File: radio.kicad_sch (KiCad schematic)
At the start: 34 parts

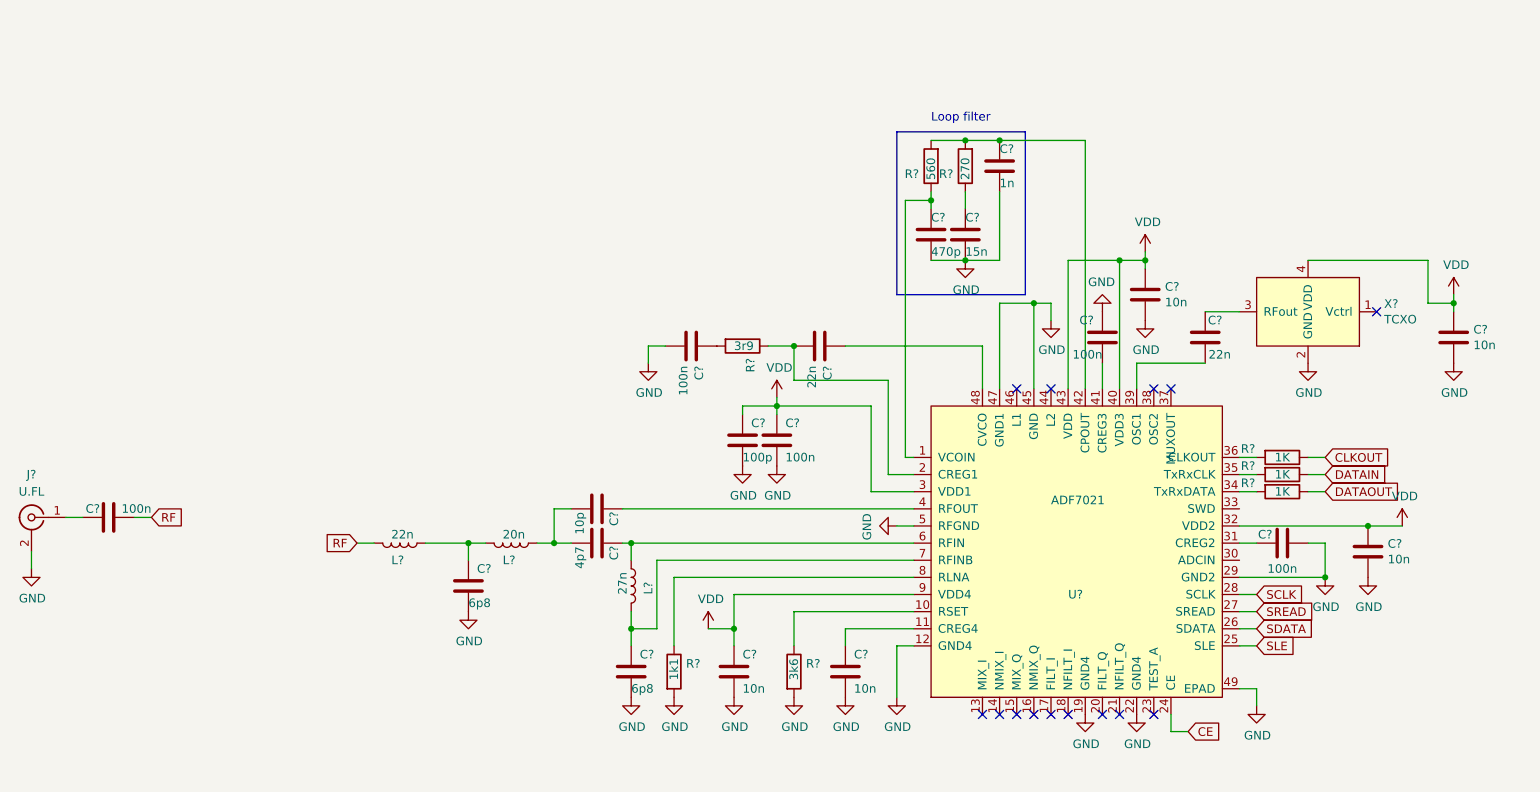
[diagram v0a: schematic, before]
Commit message: Changed MCU and M.2 pin assignment
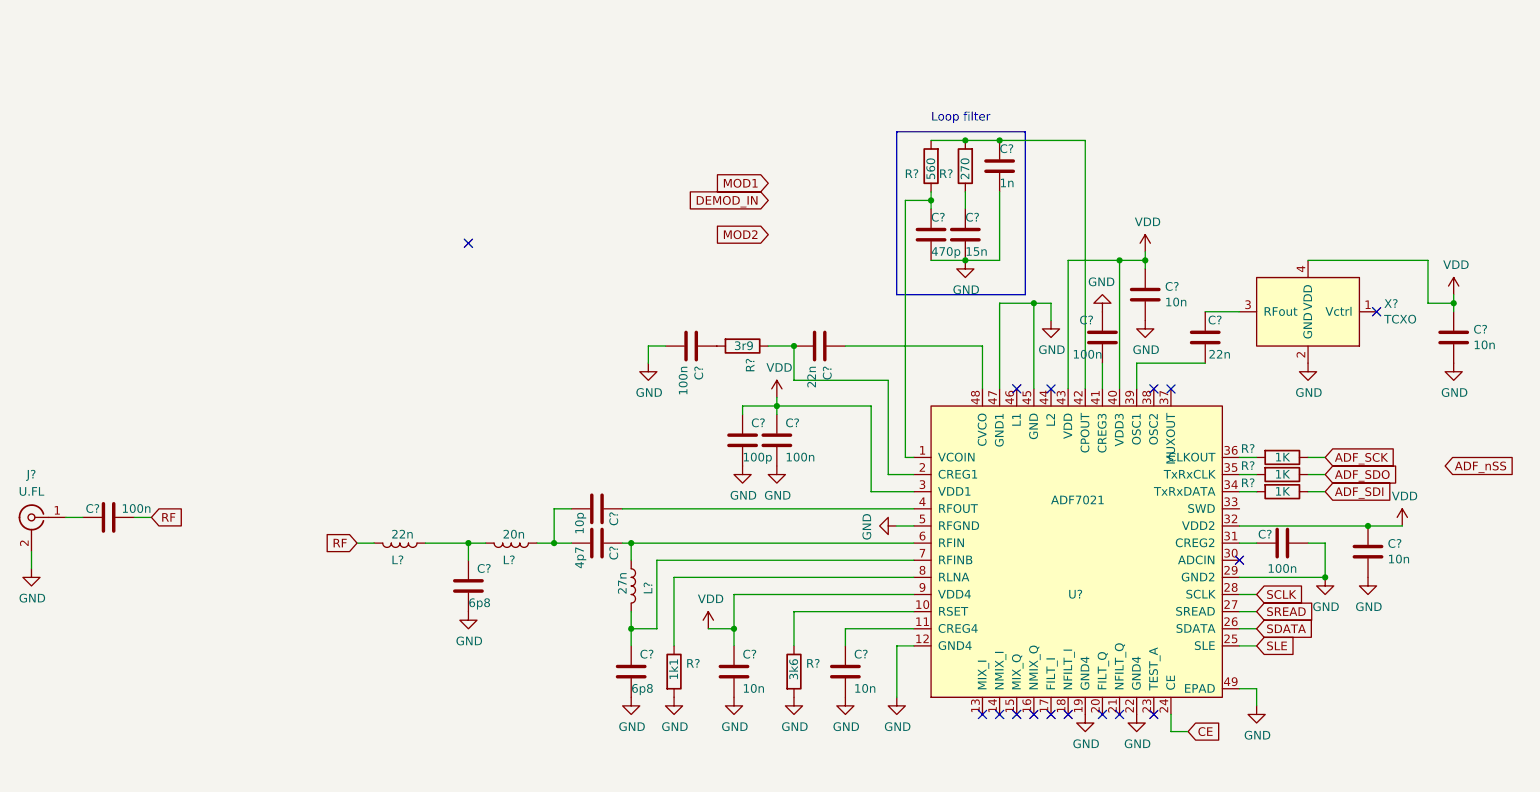
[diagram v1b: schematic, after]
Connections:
- net CLKOUT renamed ADF_SCK
- net DATAIN renamed ADF_SDO
- net DATAOUT renamed ADF_SDI
- no-connect marks 14 -> 16
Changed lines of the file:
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@@
   (junction (at 189.23 46.99) (diameter 0) (color 0 0 0 0)
   )
+  (no_connect (at 229.87 109.22))
   (no_connect (at 191.77 132.08))
   (no_connect (at 212.09 132.08))
   (no_connect (at 217.17 132.08))
+  (no_connect (at 115.57 62.23))
   (no_connect (at 196.85 132.08))
   (no_connect (at 209.55 132.08))
@@
     (effects (font (size 1.27 1.27)) (justify left bottom))
   )
-  (global_label "DATAOUT" (shape input) (at 242.57 99.06 0) (fields_autoplaced)
+  (global_label "ADF_SDO" (shape input) (at 242.57 96.52 0) (fields_autoplaced)
+    (effects (font (size 1.27 1.27)) (justify left))
+    (property "Intersheet References" "${INTERSHEET_REFS}" (id 0) (at 253.119 96.5994 0)
+      (effects (font (size 1.27 1.27)) (justify left) hide)
+    )
+  )
+  (global_label "ADF_nSS" (shape input) (at 260.35 95.25 0) (fields_autoplaced)
+    (effects (font (size 1.27 1.27)) (justify left))
+    (property "Intersheet References" "${INTERSHEET_REFS}" (id 0) (at 270.6571 95.3294 0)
+      (effects (font (size 1.27 1.27)) (justify left) hide)
+    )
+  )
+  (global_label "RF" (shape input) (at 68.58 102.87 0) (fields_autoplaced)
+    (effects (font (size 1.27 1.27)) (justify left))
+    (property "Intersheet References" "${INTERSHEET_REFS}" (id 0) (at 26.67 -25.4 0)
+      (effects (font (size 1.27 1.27)) hide)
+    )
+  )
+  (global_label "SDATA" (shape input) (at 232.41 119.38 0) (fields_autoplaced)
     (effects (font (size 1.27 1.27)) (justify left))
     (property "Intersheet References" "${INTERSHEET_REFS}" (id 0) (at 85.09 -59.69 0)
@@
     )
   )
-  (global_label "CLKOUT" (shape input) (at 242.57 93.98 0) (fields_autoplaced)
+  (global_label "DEMOD_IN" (shape input) (at 160.02 55.88 180) (fields_autoplaced)
+    (effects (font (size 1.27 1.27)) (justify right))
+    (property "Intersheet References" "${INTERSHEET_REFS}" (id 0) (at 148.322 55.8006 0)
+      (effects (font (size 1.27 1.27)) (justify right) hide)
+    )
+  )
+  (global_label "CE" (shape input) (at 222.25 134.62 0) (fields_autoplaced)
     (effects (font (size 1.27 1.27)) (justify left))
     (property "Intersheet References" "${INTERSHEET_REFS}" (id 0) (at 85.09 -59.69 0)
@@
     )
   )
-  (global_label "RF" (shape input) (at 68.58 102.87 0) (fields_autoplaced)
-    (effects (font (size 1.27 1.27)) (justify left))
-    (property "Intersheet References" "${INTERSHEET_REFS}" (id 0) (at 26.67 -25.4 0)
-      (effects (font (size 1.27 1.27)) hide)
-    )
-  )
-  (global_label "SDATA" (shape input) (at 232.41 119.38 0) (fields_autoplaced)
+  (global_label "SREAD" (shape input) (at 232.41 116.84 0) (fields_autoplaced)
     (effects (font (size 1.27 1.27)) (justify left))
     (property "Intersheet References" "${INTERSHEET_REFS}" (id 0) (at 85.09 -59.69 0)
@@
     )
   )
-  (global_label "CE" (shape input) (at 222.25 134.62 0) (fields_autoplaced)
+  (global_label "ADF_SDI" (shape input) (at 242.57 99.06 0) (fields_autoplaced)
+    (effects (font (size 1.27 1.27)) (justify left))
+    (property "Intersheet References" "${INTERSHEET_REFS}" (id 0) (at 252.3932 99.1394 0)
+      (effects (font (size 1.27 1.27)) (justify left) hide)
+    )
+  )
+  (global_label "SLE" (shape input) (at 232.41 121.92 0) (fields_autoplaced)
     (effects (font (size 1.27 1.27)) (justify left))
     (property "Intersheet References" "${INTERSHEET_REFS}" (id 0) (at 85.09 -59.69 0)
@@
     )
   )
-  (global_label "SREAD" (shape input) (at 232.41 116.84 0) (fields_autoplaced)
-    (effects (font (size 1.27 1.27)) (justify left))
-    (property "Intersheet References" "${INTERSHEET_REFS}" (id 0) (at 85.09 -59.69 0)
-      (effects (font (size 1.27 1.27)) hide)
-    )
-  )
-  (global_label "SLE" (shape input) (at 232.41 121.92 0) (fields_autoplaced)
-    (effects (font (size 1.27 1.27)) (justify left))
-    (property "Intersheet References" "${INTERSHEET_REFS}" (id 0) (at 85.09 -59.69 0)
-      (effects (font (size 1.27 1.27)) hide)
+  (global_label "MOD1" (shape input) (at 160.02 53.34 180) (fields_autoplaced)
+    (effects (font (size 1.27 1.27)) (justify right))
+    (property "Intersheet References" "${INTERSHEET_REFS}" (id 0) (at 152.4344 53.2606 0)
+      (effects (font (size 1.27 1.27)) (justify right) hide)
     )
   )
@@
     )
   )
-  (global_label "DATAIN" (shape input) (at 242.57 96.52 0) (fields_autoplaced)
-    (effects (font (size 1.27 1.27)) (justify left))
-    (property "Intersheet References" "${INTERSHEET_REFS}" (id 0) (at 85.09 -59.69 0)
-      (effects (font (size 1.27 1.27)) hide)
-    )
-  )
+  (global_label "ADF_SCK" (shape input) (at 242.57 93.98 0) (fields_autoplaced)
+    (effects (font (size 1.27 1.27)) (justify left))
+    (property "Intersheet References" "${INTERSHEET_REFS}" (id 0) (at 253.0585 94.0594 0)
+      (effects (font (size 1.27 1.27)) (justify left) hide)
+    )
+  )
+  (global_label "MOD2" (shape input) (at 160.02 60.96 180) (fields_autoplaced)
+    (effects (font (size 1.27 1.27)) (justify right))
+    (property "Intersheet References" "${INTERSHEET_REFS}" (id 0) (at 152.4344 60.8806 0)
+      (effects (font (size 1.27 1.27)) (justify right) hide)
+    )
+  )

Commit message: Add MCU to ADF7021 connection
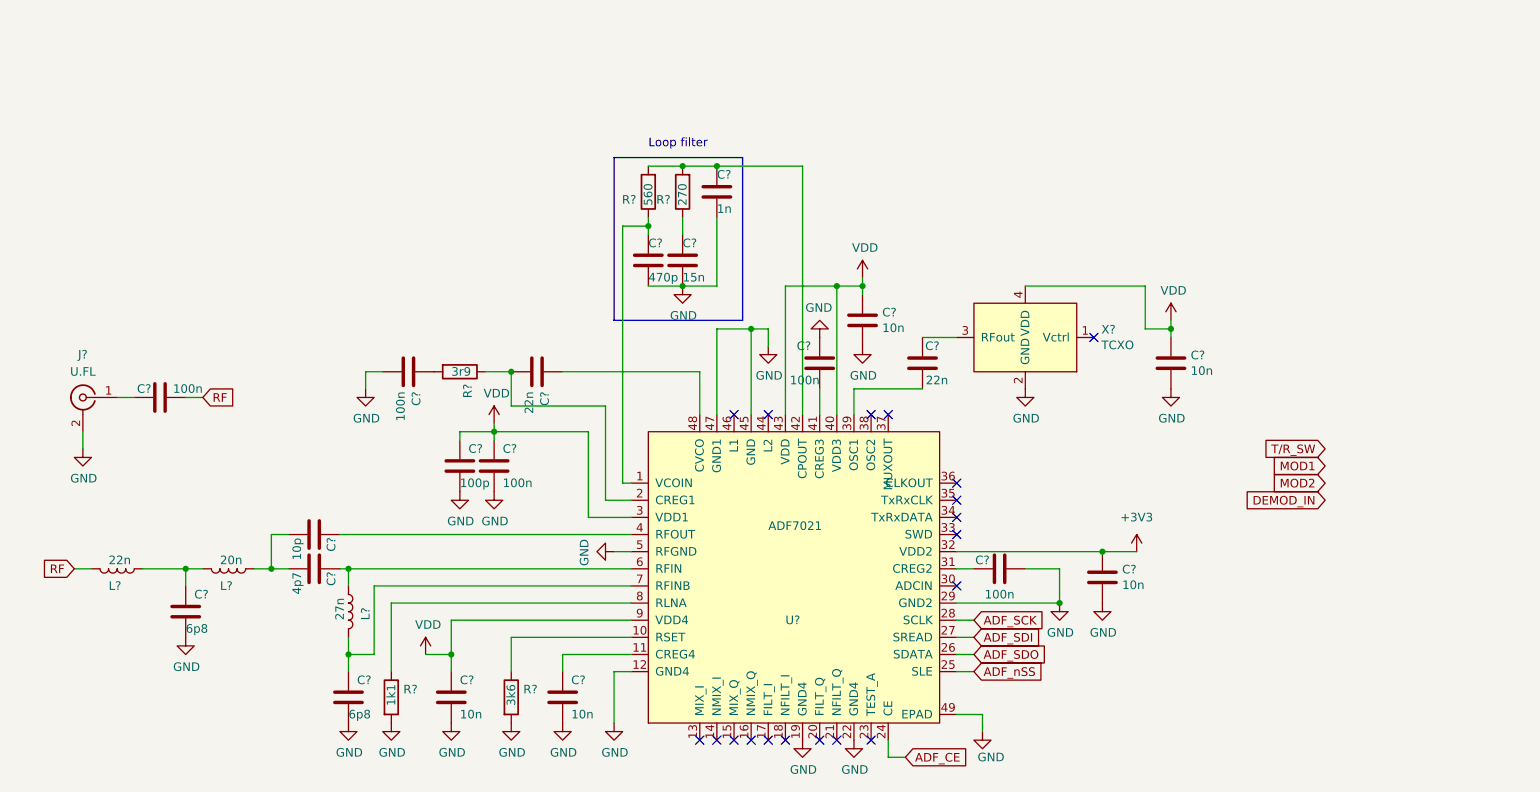
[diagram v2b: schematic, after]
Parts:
- removed R? (x3): 1K, Resistor_SMD:R_0402_1005Metric, symbol Device:R
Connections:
- net SCLK is gone; now on net ADF_SCK: U?.28 (SCLK)
- net SDATA is gone; now on net ADF_SDO: U?.26 (SDATA)
- net SLE is gone; now on net ADF_nSS: U?.25 (SLE)
- net SREAD is gone; now on net ADF_SDI: U?.27 (SREAD)
- net VDD: no longer C?.1, U?.32 (VDD2)
- net CE renamed ADF_CE
- new net +3V3: C?.1, U?.32 (VDD2)
- no-connect marks 16 -> 19
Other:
- moved on the sheet: C?, J?, L?, R?, U?, X?

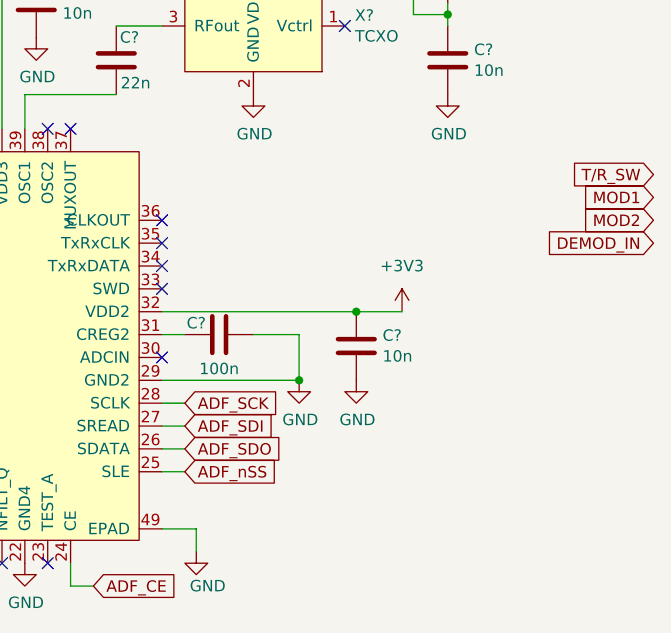
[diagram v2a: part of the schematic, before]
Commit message: Added interfacing transistors for LED and nRESET signals on M.2 connector, switched from global to hierarchical net labels
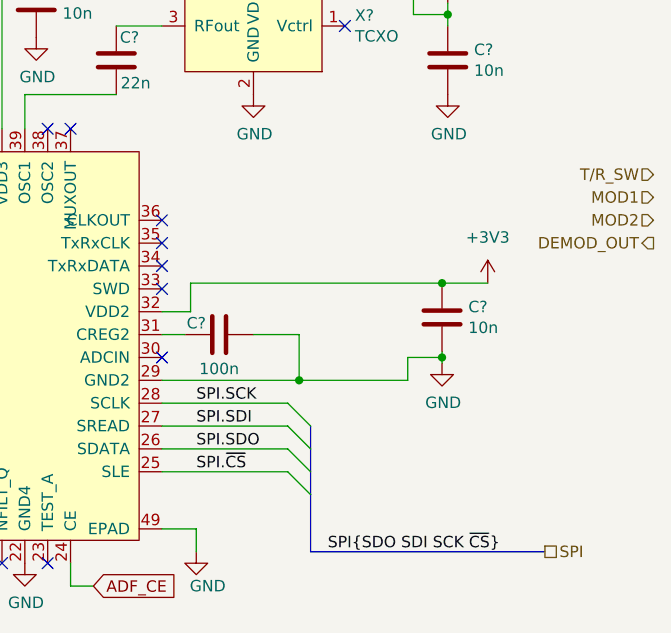
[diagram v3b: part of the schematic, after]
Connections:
- net ADF_SCK renamed SPI.SCK
- net ADF_SDI renamed SPI.SDI
- net ADF_SDO renamed SPI.SDO
- net ADF_nSS renamed SPI.~{CS}
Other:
- company: (none) -> OpenRTX & M17
- moved on the sheet: C?

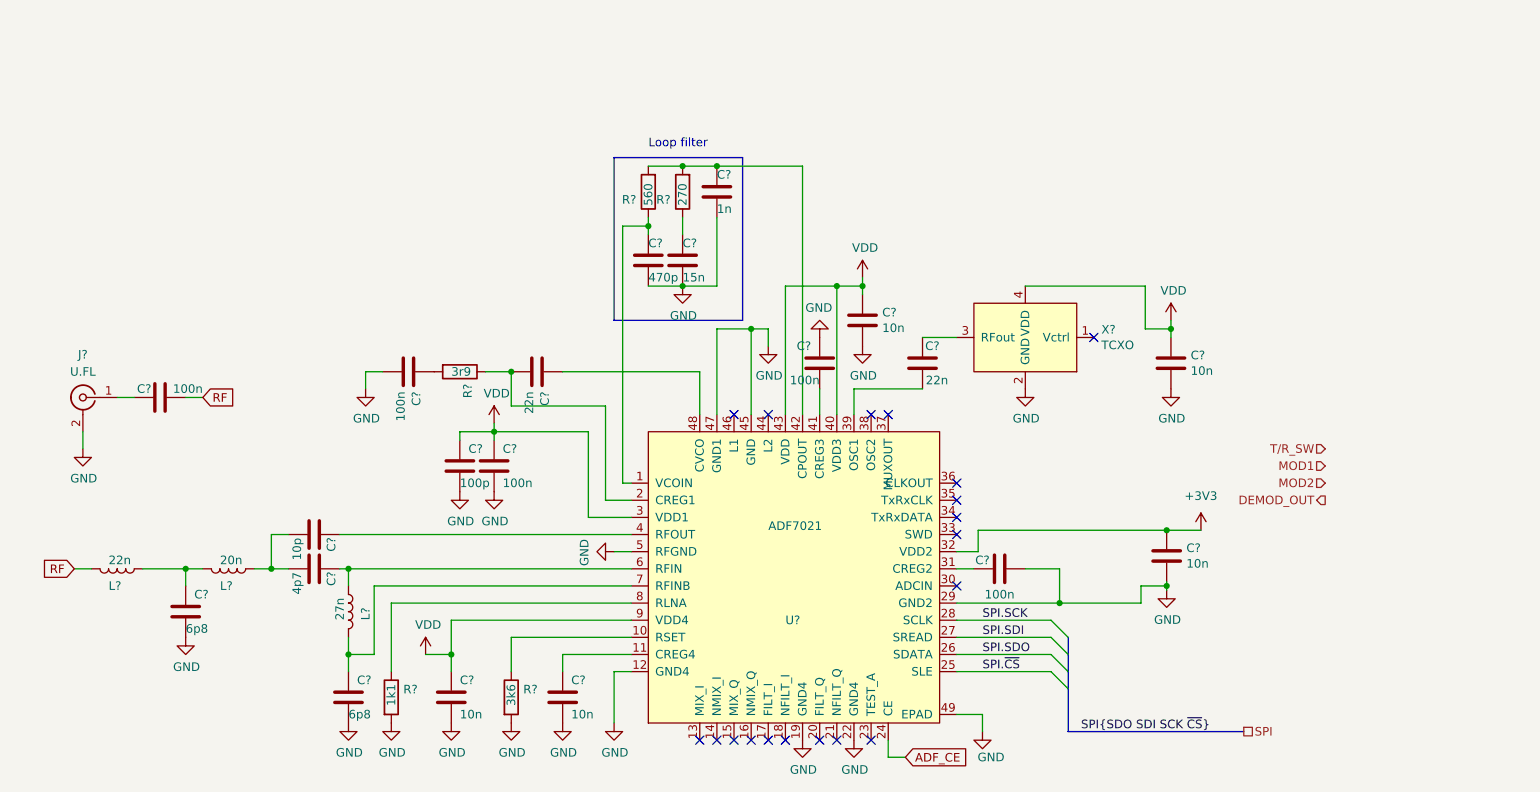
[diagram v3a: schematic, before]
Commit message: Aligned ADF7021 wiring to TR-9 schematic
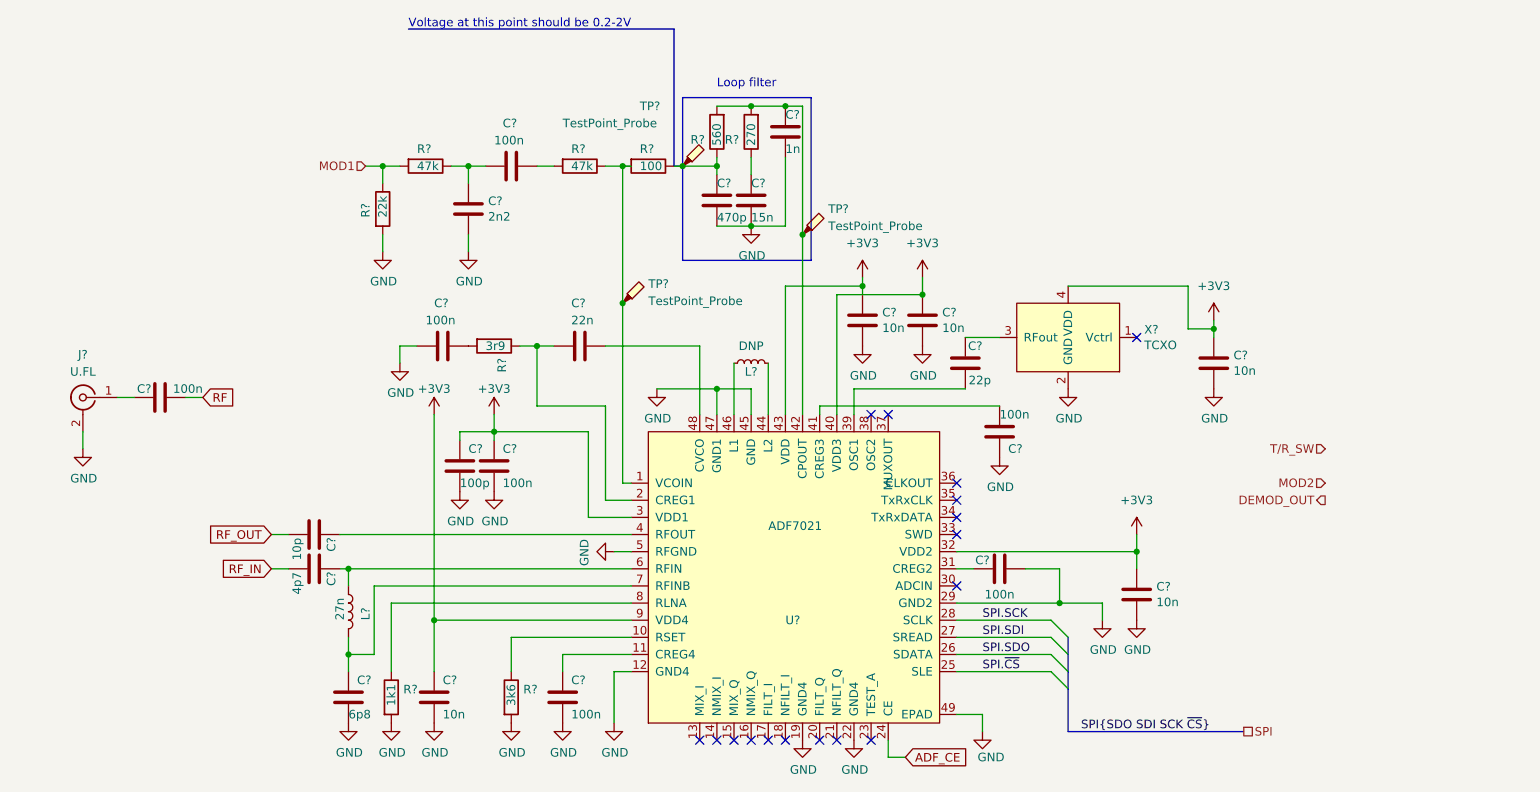
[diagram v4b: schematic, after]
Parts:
- removed C?: 6p8, Capacitor_SMD:C_0402_1005Metric, symbol Device:C
- removed L?: 20n, Inductor_SMD:L_0402_1005Metric, symbol Device:L
- removed L?: 22n, Inductor_SMD:L_0402_1005Metric, symbol Device:L
- added C?: 100n, Capacitor_SMD:C_0402_1005Metric, symbol Device:C
- added C?: 10n, Capacitor_SMD:C_0402_1005Metric, symbol Device:C
- added C?: 2n2, Capacitor_SMD:C_0402_1005Metric, symbol Device:C
- added L?: DNP, Inductor_SMD:L_0603_1608Metric, symbol Device:L_Small
- added R? (x2): 47k, Resistor_SMD:R_0402_1005Metric, symbol Device:R
- added R?: 100, Resistor_SMD:R_0402_1005Metric, symbol Device:R
- added R?: 22k, Resistor_SMD:R_0402_1005Metric, symbol Device:R
- added TP? (x3): TestPoint_Probe, symbol Connector:TestPoint_Probe
- C?: value 22n -> 22p
- C?: value 10n -> 100n
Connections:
- net VDD is gone; now on net +3V3: C?.1, C?.1, C?.1, C?.1, C?.1, U?.3 (VDD1), U?.40 (VDD3), U?.43 (VDD), U?.9 (VDD4), X?.4 (VDD)
- net +3V3: now also C?.1
- net GND: now also C?.2, C?.2, R?.2
- net MOD1: now also R?.1, R?.2
- net RF_IN: now reaches C?.1
- net RF_IN: no longer C?.1
- net at C?.1, R?.1: now also R?.1, TP?.1; no longer U?.1 (VCOIN)
- net at C?.1, R?.2, R?.2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: now also TP?.1
- net at U?.44 (L2): now also L?.2
- net at U?.46 (L1): now also L?.1
- new net: C?.1, C?.2, R?.1
- new net: R?.1, R?.2, TP?.1, U?.1 (VCOIN)
- new net: C?.1, R?.2
- new net RF_OUT: C?.1
- no-connect marks 19 -> 17
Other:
- note added: "Voltage at this point should be 0.2-2V"
- moved on the sheet: C?, R?, X?
